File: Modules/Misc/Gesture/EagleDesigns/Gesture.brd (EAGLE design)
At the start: 100 x 80 mm, 26 parts, among them Q1 16MHz, U1 NRF24L01ALT1, U2 ATMEGA328P_TQFP, U3 LSM9DS1, Y1 ANTENNA2SMD5

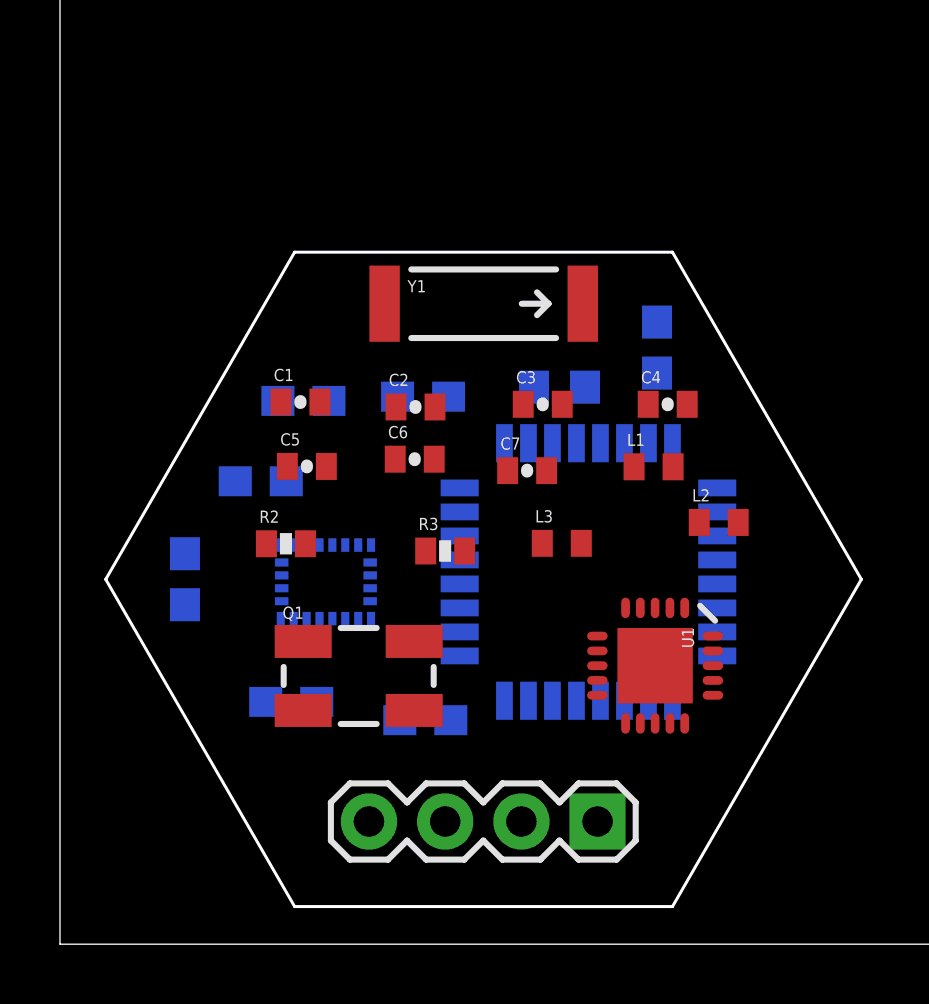
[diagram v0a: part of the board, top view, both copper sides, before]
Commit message: updated the PCB/Schematics for the Gesture module
TODO: now I only need to build the middle PCB (ATmega328p + IMU)
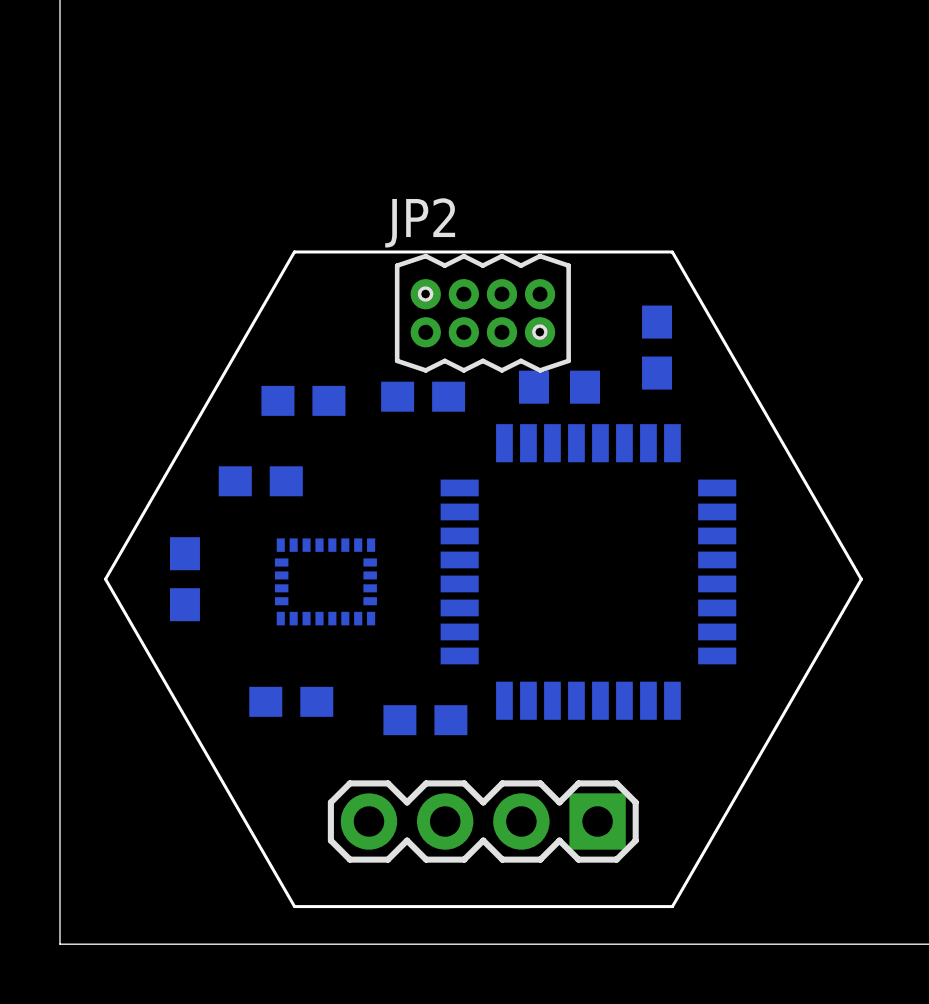
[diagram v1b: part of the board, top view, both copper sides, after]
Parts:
- removed C1, C2: 22pF, SparkFun:0402-CAP
- removed C3: 33nF, SparkFun:0402-CAP
- removed C4: 2.2nF, SparkFun:0402-CAP
- removed C5: 4.7pF, SparkFun:0402-CAP
- removed C6: 1.0pF, SparkFun:0402-CAP
- removed C7: 1.5pF, SparkFun:0402-CAP
- removed L1: 3.9nH, SparkFun:C0402
- removed L2: 2.7nH, SparkFun:C0402
- removed L3: 8.2nH, SparkFun:C0402
- removed Q1: 16MHz, SparkFun:CRYSTAL-SMD-5X3
- removed R2: 1M, SparkFun:0402-RES
- removed R3: 22K, SparkFun:0402-RES
- removed U1: NRF24L01ALT1, Testing:QFN20_ALT1
- removed Y1: ANTENNA2SMD5, SparkFun:ANTENNA-CHIP5
- added JP2: (no value), MakerWear:M04X2_0.05"
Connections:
- removed net ANT: C6.2, C7.2, Y1.FEED
- removed net N$1: C1.1, Q1.1, R2.1, U1.9
- removed net N$2: C2.1, Q1.3, R2.2, U1.10
- removed net N$3: L2.2, L3.1, U1.12
- removed net N$4: R3.1, U1.16
- removed net N$5: C3.1, U1.19
- removed net N$6: L1.1, L3.2, U1.13
- removed net N$7: C4.1, C5.1, L2.1, U1.11
- removed net N$9: C7.1, L1.2
- net CE: now also JP2.3; no longer U1.1
- net CSN: now also JP2.5; no longer U1.2
- net GND: now also JP2.2; no longer C1.2, C2.2, C3.2, C4.2, C5.2, C6.1, R3.2, U1.0, U1.14, U1.17, U1.20, U1.8
- net IRQ: now also JP2.4; no longer U1.6
- net MISO: now also JP2.6; no longer U1.5
- net MOSI: now also JP2.8; no longer U1.4
- net SCK: now also JP2.7; no longer U1.3
- net VCC: now also JP2.1; no longer U1.15, U1.18, U1.7

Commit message: finished the Gesture module
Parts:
- added JP3: (no value), SparkFun-Connectors:1X02_LOCK
- moved R4 13.1 mm to (19.3, 12.0), flipped to the top, turned to 180 degrees
- moved C10 12.8 mm to (9.27, 20.8), flipped to the top, turned to 90 degrees
- moved U3 12.6 mm to (21.0, 15.6), flipped to the top, turned to 90 degrees
- moved R1 12.4 mm to (20.9, 6.90), flipped to the top, turned to 270 degrees
- moved C12 12.1 mm to (15.4, 16.7), flipped to the top, turned to 90 degrees
- moved R5 12.0 mm to (15.7, 8.69), flipped to the top
- moved C8 9.66 mm to (10.2, 8.67), flipped to the top, turned to 270 degrees
- moved C9 9.61 mm to (12.9, 8.67), flipped to the top, turned to 270 degrees
- moved C11 9.25 mm to (12.7, 16.7), flipped to the top, turned to 90 degrees
- moved U2 5.70 mm to (11.9, 12.1), turned to 180 degrees
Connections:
- net RX: now also JP3.1
- net TX: now also JP3.2
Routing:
- net GND: track 0.00 -> 80.9 mm, vias 0 -> 1
- net VCC: track 0.00 -> 74.6 mm, vias 0 -> 1
- net 1X3SIN-SOUT: track 0.00 -> 30.3 mm
- net SDA: track 0.00 -> 19.9 mm, vias 0 -> 1
- net SCL: track 0.00 -> 17.0 mm, vias 0 -> 1
- net RX: track 0.00 -> 16.1 mm, vias 0 -> 1
- net MISO: track 0.00 -> 11.6 mm
- net SCK: track 0.00 -> 10.4 mm, vias 0 -> 1
- net IRQ: track 0.00 -> 9.77 mm
- net TX: track 0.00 -> 9.52 mm
- net MOSI: track 0.00 -> 9.06 mm
- net N$10: track 0.00 -> 8.25 mm
- net CSN: track 0.00 -> 4.67 mm
- net CE: track 0.00 -> 4.47 mm
- net N$8: track 0.00 -> 4.35 mm

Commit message: another round of minor fixes
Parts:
- JP3: device SparkFun-Connectors:1X02_LOCK -> SparkFun-Connectors:1X03
- moved JP3 1.39 mm to (4.67, 14.7)
- moved U2 0.69 mm to (12.5, 12.5)
- moved R1 0.48 mm to (20.9, 6.41)
- moved R4 0.37 mm to (19.6, 11.8)
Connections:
- net RESET: now also JP3.3
- net RX: now also JP3.2; no longer JP3.1
- net TX: now also JP3.1; no longer JP3.2
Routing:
- net RESET: track 0.00 -> 12.7 mm
- net VCC: track 74.6 -> 82.5 mm, vias 1 -> 2
- net TX: track 9.52 -> 14.5 mm, vias 0 -> 1
- net GND: track 80.9 -> 85.9 mm
- net RX: track 16.1 -> 13.1 mm, vias 1 -> 0
- net SDA: track 19.9 -> 21.7 mm
- net SCK: track 10.4 -> 9.18 mm
- net SCL: track 17.0 -> 15.8 mm
- net 1X3SIN-SOUT: track 30.3 -> 29.3 mm
- net CSN: track 4.67 -> 3.99 mm

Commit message: unknown changes! :(
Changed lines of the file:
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@@
 <grid distance="0.0127" unitdist="mm" unit="mm" style="lines" multiple="1" display="no" altdistance="0.00635" altunitdist="mm" altunit="mm"/>
 <layers>
-<layer number="1" name="Top" color="4" fill="1" visible="yes" active="yes"/>
+<layer number="1" name="Top" color="4" fill="1" visible="no" active="yes"/>
 <layer number="2" name="Route2" color="1" fill="3" visible="no" active="no"/>
 <layer number="15" name="Route15" color="4" fill="6" visible="no" active="no"/>
@@
 <wire x1="10.2743" y1="2.286" x2="10.2743" y2="4.064" width="0.254" layer="1"/>
 <wire x1="10.2743" y1="4.064" x2="10.2997" y2="4.0894" width="0.254" layer="1"/>
-<wire x1="16.7513" y1="10.5476" x2="17.812" y2="10.5476" width="0.254" layer="16"/>
-<wire x1="17.812" y1="10.5476" x2="18.2499" y2="10.9855" width="0.254" layer="16"/>
-<wire x1="18.2499" y1="10.9855" x2="19.9263" y2="10.9855" width="0.254" layer="16"/>
+<wire x1="16.7513" y1="10.5476" x2="17.7485" y2="10.5476" width="0.254" layer="16"/>
+<wire x1="17.7485" y1="10.5476" x2="18.1864" y2="10.9855" width="0.254" layer="16"/>
+<wire x1="18.1864" y1="10.9855" x2="19.9263" y2="10.9855" width="0.254" layer="16"/>
 <wire x1="19.9263" y1="10.9855" x2="20.8534" y2="10.0457" width="0.254" layer="16"/>
 <wire x1="20.8534" y1="10.0457" x2="20.8534" y2="4.3688" width="0.254" layer="16"/>
@@
 <wire x1="14.732" y1="22.479" x2="14.9352" y2="22.6822" width="0.254" layer="16"/>
 <wire x1="14.9352" y1="22.6822" x2="17.272" y2="22.6822" width="0.254" layer="16"/>
-<wire x1="17.272" y1="22.6822" x2="17.6149" y2="22.3393" width="0.254" layer="16"/>
-<wire x1="17.6149" y1="22.3393" x2="17.6149" y2="18.0086" width="0.254" layer="16"/>
-<wire x1="17.6149" y1="18.0086" x2="16.4592" y2="16.8402" width="0.254" layer="16"/>
+<wire x1="17.272" y1="22.6822" x2="17.7419" y2="22.3393" width="0.254" layer="16"/>
+<wire x1="17.7419" y1="22.3393" x2="17.7419" y2="18.0086" width="0.254" layer="16"/>
+<wire x1="17.7419" y1="18.0086" x2="16.4592" y2="16.8402" width="0.254" layer="16"/>
 <wire x1="16.4592" y1="16.8402" x2="15.2587" y2="16.8402" width="0.254" layer="16"/>
 </signal>
@@
 <contactref element="U2" pad="30"/>
 <contactref element="JP3" pad="2"/>
-<wire x1="11.2587" y1="8.255" x2="11.2587" y2="6.4708" width="0.254" layer="16"/>
-<wire x1="11.2587" y1="6.4708" x2="11.0998" y2="6.2865" width="0.254" layer="16"/>
-<wire x1="11.0998" y1="6.2865" x2="6.8072" y2="6.2865" width="0.254" layer="16"/>
-<wire x1="6.8072" y1="6.2865" x2="6.604" y2="6.4897" width="0.254" layer="16"/>
-<wire x1="6.604" y1="6.4897" x2="6.604" y2="10.2235" width="0.254" layer="16"/>
+<wire x1="11.2587" y1="8.255" x2="11.2587" y2="6.4962" width="0.254" layer="16"/>
+<wire x1="11.2587" y1="6.4962" x2="11.1125" y2="6.3373" width="0.254" layer="16"/>
+<wire x1="11.1125" y1="6.3373" x2="6.8199" y2="6.3373" width="0.254" layer="16"/>
+<wire x1="6.8199" y1="6.3373" x2="6.604" y2="6.5532" width="0.254" layer="16"/>
+<wire x1="6.604" y1="6.5532" x2="6.604" y2="10.2235" width="0.254" layer="16"/>
 <wire x1="6.604" y1="10.2235" x2="4.6736" y2="12.1539" width="0.254" layer="16"/>
 </signal>
@@
 <wire x1="7.5692" y1="14.3383" x2="7.5692" y2="7.7343" width="0.254" layer="1"/>
 <via x="7.5692" y="7.7343" extent="1-16" drill="0.3"/>
-<wire x1="7.5692" y1="7.7343" x2="7.5692" y2="7.0993" width="0.254" layer="16"/>
-<wire x1="7.5692" y1="7.0993" x2="7.7597" y2="6.9088" width="0.254" layer="16"/>
-<wire x1="7.7597" y1="6.9088" x2="10.3251" y2="6.9088" width="0.254" layer="16"/>
-<wire x1="10.3251" y1="6.9088" x2="10.4902" y2="7.0739" width="0.254" layer="16"/>
-<wire x1="10.4902" y1="7.0739" x2="10.4902" y2="7.7917" width="0.254" layer="16"/>
-<wire x1="10.4902" y1="7.7917" x2="10.4587" y2="8.255" width="0.254" layer="16"/>
+<wire x1="7.5692" y1="7.7343" x2="7.5692" y2="7.1501" width="0.254" layer="16"/>
+<wire x1="7.5692" y1="7.1501" x2="7.7089" y2="6.9723" width="0.254" layer="16"/>
+<wire x1="7.7089" y1="6.9723" x2="10.2743" y2="6.9723" width="0.254" layer="16"/>
+<wire x1="10.2743" y1="6.9723" x2="10.4521" y2="7.112" width="0.254" layer="16"/>
+<wire x1="10.4521" y1="7.112" x2="10.4521" y2="7.8298" width="0.254" layer="16"/>
+<wire x1="10.4521" y1="7.8298" x2="10.4587" y2="8.255" width="0.254" layer="16"/>
 </signal>
 </signals>
